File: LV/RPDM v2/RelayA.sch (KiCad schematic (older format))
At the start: 6 parts, among them K2 G8NW, Q2 Q_Dual_NMOS

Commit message: rPDM - Started on board layout
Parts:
- D4: renamed from D21; footprint (none) -> Diode_UOWM:TO-277_FSV10150V
- D5: renamed from D22; footprint (none) -> Diode_UOWM:TO-277_FSV10150V
- renumbered K2 to K3, Q2 to Q3, R24 to R14, R25 to R15
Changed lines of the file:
@@
 $Descr A4 11693 8268
 encoding utf-8
-Sheet 25 32
+Sheet 9 32
 Title "Relay Circuit"
 Date "2021-06-28"
@@
 Output
 $Comp
-L power:GND #PWR031
+L power:GND #PWR020
 U 1 1 6114E9D0
 P 6000 5000
-AR Path="/5E554D5D/5E5E9CA9/6114E9D0" Ref="#PWR031"  Part="1"
+AR Path="/5E554D5D/5E5E9CA9/6114E9D0" Ref="#PWR020"  Part="1"
 AR Path="/5E554D5D/5E5A0290/6114E9D0" Ref="#PWR?"  Part="1"
 AR Path="/5E554D5D/5E5A035E/6114E9D0" Ref="#PWR?"  Part="1"
@@
 AR Path="/5E554D5D/60DE7FBD/6114E9D0" Ref="#PWR?"  Part="1"
 AR Path="/5E554D5D/60DE88EB/6114E9D0" Ref="#PWR?"  Part="1"
-AR Path="/5E554D5D/60DED789/6114E9D0" Ref="#PWR026"  Part="1"
+AR Path="/5E554D5D/60DED789/6114E9D0" Ref="#PWR014"  Part="1"
 AR Path="/5E554D5D/60DEDCB5/6114E9D0" Ref="#PWR?"  Part="1"
 AR Path="/60E5EBEF/6114E9D0" Ref="#PWR?"  Part="1"
-F 0 "#PWR026" H 6000 4750 50  0001 C CNN
+F 0 "#PWR020" H 6000 4750 50  0001 C CNN
 F 1 "GND" H 6005 4827 50  0000 C CNN
 F 2 "" H 6000 5000 50  0001 C CNN
@@
 	6000 5000 6000 4700
 $Comp
-L Device2:R R24
+L Device2:R R14
 U 1 1 6183CC28
 P 5000 4750
-AR Path="/5E554D5D/5E5E9CA9/6183CC28" Ref="R24"  Part="1"
-AR Path="/5E554D5D/60DED789/6183CC28" Ref="R21"  Part="1"
+AR Path="/5E554D5D/5E5E9CA9/6183CC28" Ref="R14"  Part="1"
+AR Path="/5E554D5D/60DED789/6183CC28" Ref="R10"  Part="1"
 AR Path="/5E554D5D/60DE88EB/6183CC28" Ref="R?"  Part="1"
 AR Path="/5E554D5D/60DEDCB5/6183CC28" Ref="R?"  Part="1"
-F 0 "R21" H 5070 4796 50  0000 L CNN
+F 0 "R14" H 5070 4796 50  0000 L CNN
 F 1 "100k" H 5070 4705 50  0000 L CNN
 F 2 "Resistor_SMD:R_0805_2012Metric_Pad1.15x1.40mm_HandSolder" V 4930 4750 50  0001 C CNN
@@
 	5000 4900 5000 5000
 $Comp
-L power:GND #PWR030
+L power:GND #PWR019
 U 1 1 6114E9D3
 P 5000 5000
-AR Path="/5E554D5D/5E5E9CA9/6114E9D3" Ref="#PWR030"  Part="1"
+AR Path="/5E554D5D/5E5E9CA9/6114E9D3" Ref="#PWR019"  Part="1"
 AR Path="/5E554D5D/5E5A0290/6114E9D3" Ref="#PWR?"  Part="1"
 AR Path="/5E554D5D/5E5A035E/6114E9D3" Ref="#PWR?"  Part="1"
@@
 AR Path="/5E554D5D/60DE7FBD/6114E9D3" Ref="#PWR?"  Part="1"
 AR Path="/5E554D5D/60DE88EB/6114E9D3" Ref="#PWR?"  Part="1"
-AR Path="/5E554D5D/60DED789/6114E9D3" Ref="#PWR025"  Part="1"
+AR Path="/5E554D5D/60DED789/6114E9D3" Ref="#PWR013"  Part="1"
 AR Path="/5E554D5D/60DEDCB5/6114E9D3" Ref="#PWR?"  Part="1"
 AR Path="/60E5EBEF/6114E9D3" Ref="#PWR?"  Part="1"
-F 0 "#PWR025" H 5000 4750 50  0001 C CNN
+F 0 "#PWR019" H 5000 4750 50  0001 C CNN
 F 1 "GND" H 5005 4827 50  0000 C CNN
 F 2 "" H 5000 5000 50  0001 C CNN
@@
 	5000 4600 5000 4500
 $Comp
-L Device2:Q_Dual_NMOS_S1G1S2G2D2D2D1D1 Q2
+L Device2:Q_Dual_NMOS_S1G1S2G2D2D2D1D1 Q3
 U 1 1 6114E9D1
 P 5900 4500
-AR Path="/5E554D5D/5E5E9CA9/6114E9D1" Ref="Q2"  Part="1"
+AR Path="/5E554D5D/5E5E9CA9/6114E9D1" Ref="Q3"  Part="1"
 AR Path="/5E554D5D/60DE88EB/6114E9D1" Ref="Q?"  Part="1"
-AR Path="/5E554D5D/60DED789/6114E9D1" Ref="Q1"  Part="1"
-F 0 "Q1" H 6188 4546 50  0000 L CNN
+AR Path="/5E554D5D/60DED789/6114E9D1" Ref="Q2"  Part="1"
+F 0 "Q3" H 6188 4546 50  0000 L CNN
 F 1 "Q_Dual_NMOS" H 6188 4455 50  0000 L CNN
 F 2 "" H 6100 4500 50  0001 C CNN
@@
 $EndComp
 $Comp
-L relay_omron:G8NW K2
+L relay_omron:G8NW K3
 U 1 1 61724099
 P 5500 3300
-AR Path="/5E554D5D/5E5E9CA9/61724099" Ref="K2"  Part="1"
-AR Path="/5E554D5D/60DED789/61724099" Ref="K1"  Part="1"
-F 0 "K1" V 6067 3300 50  0000 C CNN
+AR Path="/5E554D5D/5E5E9CA9/61724099" Ref="K3"  Part="1"
+AR Path="/5E554D5D/60DED789/61724099" Ref="K2"  Part="1"
+F 0 "K3" V 6067 3300 50  0000 C CNN
 F 1 "G8NW" V 5976 3300 50  0000 C CNN
 F 2 "" H 5900 3200 50  0001 L CNN
@@
 $EndComp
 $Comp
-L Device2:R R25
+L Device2:R R15
 U 1 1 6174AD0B
 P 5500 4500
-AR Path="/5E554D5D/5E5E9CA9/6174AD0B" Ref="R25"  Part="1"
-AR Path="/5E554D5D/60DED789/6174AD0B" Ref="R22"  Part="1"
-F 0 "R22" V 5293 4500 50  0000 C CNN
+AR Path="/5E554D5D/5E5E9CA9/6174AD0B" Ref="R15"  Part="1"
+AR Path="/5E554D5D/60DED789/6174AD0B" Ref="R11"  Part="1"
+F 0 "R15" V 5293 4500 50  0000 C CNN
 F 1 "470" V 5384 4500 50  0000 C CNN
 F 2 "Resistor_SMD:R_0805_2012Metric_Pad1.15x1.40mm_HandSolder" V 5430 4500 50  0001 C CNN
@@
 $EndComp
 $Comp
-L power:GND #PWR032
+L power:GND #PWR021
 U 1 1 617CD98D
 P 6500 4000
-AR Path="/5E554D5D/5E5E9CA9/617CD98D" Ref="#PWR032"  Part="1"
+AR Path="/5E554D5D/5E5E9CA9/617CD98D" Ref="#PWR021"  Part="1"
 AR Path="/5E554D5D/5E5A0290/617CD98D" Ref="#PWR?"  Part="1"
 AR Path="/5E554D5D/5E5A035E/617CD98D" Ref="#PWR?"  Part="1"
@@
 AR Path="/5E554D5D/60DE7FBD/617CD98D" Ref="#PWR?"  Part="1"
 AR Path="/5E554D5D/60DE88EB/617CD98D" Ref="#PWR?"  Part="1"
-AR Path="/5E554D5D/60DED789/617CD98D" Ref="#PWR027"  Part="1"
+AR Path="/5E554D5D/60DED789/617CD98D" Ref="#PWR015"  Part="1"
 AR Path="/5E554D5D/60DEDCB5/617CD98D" Ref="#PWR?"  Part="1"
 AR Path="/60E5EBEF/617CD98D" Ref="#PWR?"  Part="1"
-F 0 "#PWR027" H 6500 3750 50  0001 C CNN
+F 0 "#PWR021" H 6500 3750 50  0001 C CNN
 F 1 "GND" H 6505 3827 50  0000 C CNN
 F 2 "" H 6500 4000 50  0001 C CNN
@@
 $EndComp
 $Comp
-L Device2:D_Schottky_AAK D21
+L Device2:D_Schottky_AAK D4
 U 1 1 617CF33C
 P 5500 4000
-AR Path="/5E554D5D/60DED789/617CF33C" Ref="D21"  Part="1"
-AR Path="/5E554D5D/5E5E9CA9/617CF33C" Ref="D24"  Part="1"
-F 0 "D21" H 5500 4100 50  0000 C CNN
+AR Path="/5E554D5D/60DED789/617CF33C" Ref="D4"  Part="1"
+AR Path="/5E554D5D/5E5E9CA9/617CF33C" Ref="D8"  Part="1"
+F 0 "D8" H 5500 4100 50  0000 C CNN
 F 1 "D_Schottky_Flyback" H 5450 3900 50  0000 C CNN
-F 2 "" H 5500 4000 50  0001 C CNN
+F 2 "Diode_UOWM:TO-277_FSV10150V" H 5500 4000 50  0001 C CNN
 F 3 "~" H 5500 4000 50  0001 C CNN
 	1    5500 4000
@@
 $EndComp
 $Comp
-L Device2:D_Schottky_AAK D22
+L Device2:D_Schottky_AAK D5
 U 1 1 617CFABC
 P 6500 3500
-AR Path="/5E554D5D/60DED789/617CFABC" Ref="D22"  Part="1"
-AR Path="/5E554D5D/5E5E9CA9/617CFABC" Ref="D25"  Part="1"
-F 0 "D22" V 6479 3644 50  0000 L CNN
+AR Path="/5E554D5D/60DED789/617CFABC" Ref="D5"  Part="1"
+AR Path="/5E554D5D/5E5E9CA9/617CFABC" Ref="D9"  Part="1"
+F 0 "D9" V 6479 3644 50  0000 L CNN
 F 1 "D_Schottky_Flyback" V 6570 3644 50  0000 L CNN
-F 2 "" H 6500 3500 50  0001 C CNN
+F 2 "Diode_UOWM:TO-277_FSV10150V" H 6500 3500 50  0001 C CNN
 F 3 "~" H 6500 3500 50  0001 C CNN
 	1    6500 3500

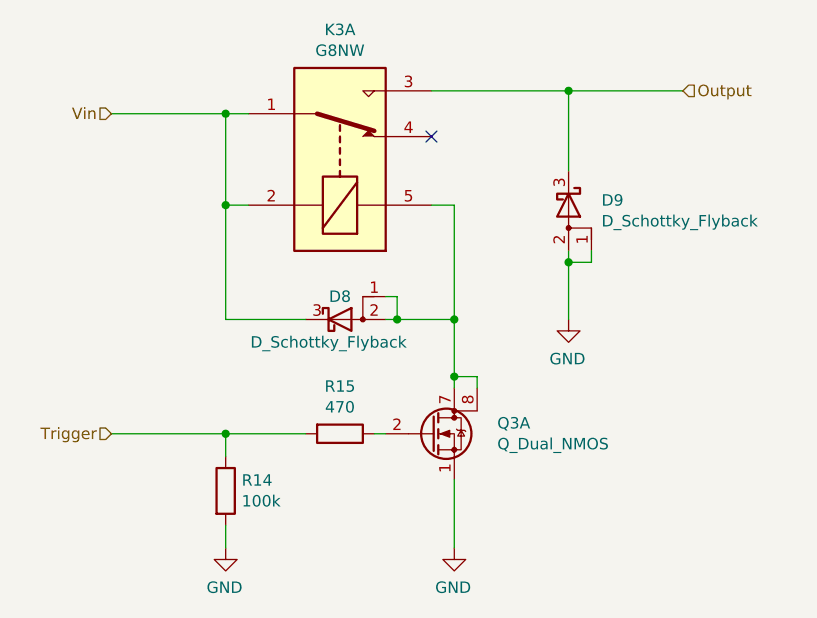
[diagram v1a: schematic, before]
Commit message: rpdm, libraries cleanup
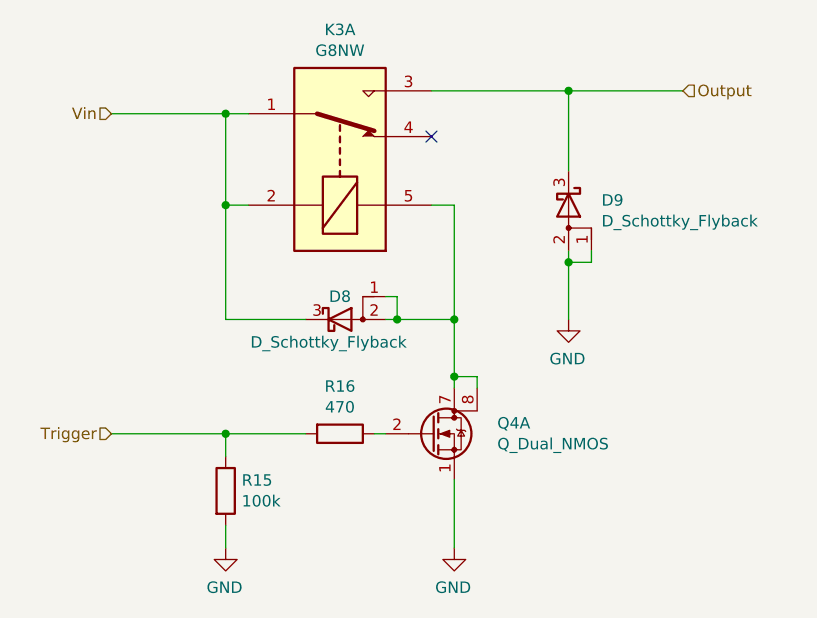
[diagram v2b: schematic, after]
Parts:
- renumbered Q3 to Q4, R14 to R15, R15 to R16
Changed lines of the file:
@@
 	6000 5000 6000 4700
 $Comp
-L Device2:R R14
+L Device2:R R15
 U 1 1 6183CC28
 P 5000 4750
-AR Path="/5E554D5D/5E5E9CA9/6183CC28" Ref="R14"  Part="1"
-AR Path="/5E554D5D/60DED789/6183CC28" Ref="R10"  Part="1"
+AR Path="/5E554D5D/5E5E9CA9/6183CC28" Ref="R15"  Part="1"
+AR Path="/5E554D5D/60DED789/6183CC28" Ref="R11"  Part="1"
 AR Path="/5E554D5D/60DE88EB/6183CC28" Ref="R?"  Part="1"
 AR Path="/5E554D5D/60DEDCB5/6183CC28" Ref="R?"  Part="1"
-F 0 "R14" H 5070 4796 50  0000 L CNN
+F 0 "R15" H 5070 4796 50  0000 L CNN
 F 1 "100k" H 5070 4705 50  0000 L CNN
 F 2 "Resistor_SMD:R_0805_2012Metric_Pad1.15x1.40mm_HandSolder" V 4930 4750 50  0001 C CNN
@@
 	5000 4600 5000 4500
 $Comp
-L Device2:Q_Dual_NMOS_S1G1S2G2D2D2D1D1 Q3
+L Device2:Q_Dual_NMOS_S1G1S2G2D2D2D1D1 Q4
 U 1 1 6114E9D1
 P 5900 4500
-AR Path="/5E554D5D/5E5E9CA9/6114E9D1" Ref="Q3"  Part="1"
+AR Path="/5E554D5D/5E5E9CA9/6114E9D1" Ref="Q4"  Part="1"
 AR Path="/5E554D5D/60DE88EB/6114E9D1" Ref="Q?"  Part="1"
-AR Path="/5E554D5D/60DED789/6114E9D1" Ref="Q2"  Part="1"
-F 0 "Q3" H 6188 4546 50  0000 L CNN
+AR Path="/5E554D5D/60DED789/6114E9D1" Ref="Q3"  Part="1"
+F 0 "Q4" H 6188 4546 50  0000 L CNN
 F 1 "Q_Dual_NMOS" H 6188 4455 50  0000 L CNN
 F 2 "" H 6100 4500 50  0001 C CNN
@@
 $EndComp
 $Comp
-L Device2:R R15
+L Device2:R R16
 U 1 1 6174AD0B
 P 5500 4500
-AR Path="/5E554D5D/5E5E9CA9/6174AD0B" Ref="R15"  Part="1"
-AR Path="/5E554D5D/60DED789/6174AD0B" Ref="R11"  Part="1"
-F 0 "R15" V 5293 4500 50  0000 C CNN
+AR Path="/5E554D5D/5E5E9CA9/6174AD0B" Ref="R16"  Part="1"
+AR Path="/5E554D5D/60DED789/6174AD0B" Ref="R12"  Part="1"
+F 0 "R16" V 5293 4500 50  0000 C CNN
 F 1 "470" V 5384 4500 50  0000 C CNN
 F 2 "Resistor_SMD:R_0805_2012Metric_Pad1.15x1.40mm_HandSolder" V 5430 4500 50  0001 C CNN

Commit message: RPDM
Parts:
- D1: renamed from D4; footprint Diode_UOWM:TO-277_FSV10150V -> UOWM_Diodes:TO-277_FSV10150V
- D2: renamed from D5; footprint Diode_UOWM:TO-277_FSV10150V -> UOWM_Diodes:TO-277_FSV10150V
- K2: renamed from K3; footprint (none) -> UOWM_Relays:Omron-G8NW-2L-AS_SK-MFG
- Q3: renamed from Q4; footprint (none) -> UOWM_Package_SO:Diodes_SO-8_5.3x6.2mm_P1.27mm
- renumbered R15 to R12, R16 to R13
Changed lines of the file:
@@
 $Descr A4 11693 8268
 encoding utf-8
-Sheet 9 32
+Sheet 29 30
 Title "Relay Circuit"
 Date "2021-06-28"
@@
 Output
 $Comp
-L power:GND #PWR020
+L power:GND #PWR017
 U 1 1 6114E9D0
 P 6000 5000
-AR Path="/5E554D5D/5E5E9CA9/6114E9D0" Ref="#PWR020"  Part="1"
+AR Path="/5E554D5D/5E5E9CA9/6114E9D0" Ref="#PWR017"  Part="1"
 AR Path="/5E554D5D/5E5A0290/6114E9D0" Ref="#PWR?"  Part="1"
 AR Path="/5E554D5D/5E5A035E/6114E9D0" Ref="#PWR?"  Part="1"
@@
 AR Path="/5E554D5D/60DE7FBD/6114E9D0" Ref="#PWR?"  Part="1"
 AR Path="/5E554D5D/60DE88EB/6114E9D0" Ref="#PWR?"  Part="1"
-AR Path="/5E554D5D/60DED789/6114E9D0" Ref="#PWR014"  Part="1"
+AR Path="/5E554D5D/60DED789/6114E9D0" Ref="#PWR011"  Part="1"
 AR Path="/5E554D5D/60DEDCB5/6114E9D0" Ref="#PWR?"  Part="1"
 AR Path="/60E5EBEF/6114E9D0" Ref="#PWR?"  Part="1"
-F 0 "#PWR020" H 6000 4750 50  0001 C CNN
+F 0 "#PWR017" H 6000 4750 50  0001 C CNN
 F 1 "GND" H 6005 4827 50  0000 C CNN
 F 2 "" H 6000 5000 50  0001 C CNN
@@
 	6000 5000 6000 4700
 $Comp
-L Device2:R R15
+L Device2:R R12
 U 1 1 6183CC28
 P 5000 4750
-AR Path="/5E554D5D/5E5E9CA9/6183CC28" Ref="R15"  Part="1"
-AR Path="/5E554D5D/60DED789/6183CC28" Ref="R11"  Part="1"
+AR Path="/5E554D5D/5E5E9CA9/6183CC28" Ref="R12"  Part="1"
+AR Path="/5E554D5D/60DED789/6183CC28" Ref="R8"  Part="1"
 AR Path="/5E554D5D/60DE88EB/6183CC28" Ref="R?"  Part="1"
 AR Path="/5E554D5D/60DEDCB5/6183CC28" Ref="R?"  Part="1"
-F 0 "R15" H 5070 4796 50  0000 L CNN
+F 0 "R12" H 5070 4796 50  0000 L CNN
 F 1 "100k" H 5070 4705 50  0000 L CNN
 F 2 "Resistor_SMD:R_0805_2012Metric_Pad1.15x1.40mm_HandSolder" V 4930 4750 50  0001 C CNN
-F 3 "~" H 5000 4750 50  0001 C CNN
+F 3 "https://www.koaspeer.com/pdfs/RK73H.pdf" H 5000 4750 50  0001 C CNN
 	1    5000 4750
 	1    0    0    -1
@@
 	5000 4900 5000 5000
 $Comp
-L power:GND #PWR019
+L power:GND #PWR016
 U 1 1 6114E9D3
 P 5000 5000
-AR Path="/5E554D5D/5E5E9CA9/6114E9D3" Ref="#PWR019"  Part="1"
+AR Path="/5E554D5D/5E5E9CA9/6114E9D3" Ref="#PWR016"  Part="1"
 AR Path="/5E554D5D/5E5A0290/6114E9D3" Ref="#PWR?"  Part="1"
 AR Path="/5E554D5D/5E5A035E/6114E9D3" Ref="#PWR?"  Part="1"
@@
 AR Path="/5E554D5D/60DE7FBD/6114E9D3" Ref="#PWR?"  Part="1"
 AR Path="/5E554D5D/60DE88EB/6114E9D3" Ref="#PWR?"  Part="1"
-AR Path="/5E554D5D/60DED789/6114E9D3" Ref="#PWR013"  Part="1"
+AR Path="/5E554D5D/60DED789/6114E9D3" Ref="#PWR010"  Part="1"
 AR Path="/5E554D5D/60DEDCB5/6114E9D3" Ref="#PWR?"  Part="1"
 AR Path="/60E5EBEF/6114E9D3" Ref="#PWR?"  Part="1"
-F 0 "#PWR019" H 5000 4750 50  0001 C CNN
+F 0 "#PWR016" H 5000 4750 50  0001 C CNN
 F 1 "GND" H 5005 4827 50  0000 C CNN
 F 2 "" H 5000 5000 50  0001 C CNN
@@
 	5000 4600 5000 4500
 $Comp
-L Device2:Q_Dual_NMOS_S1G1S2G2D2D2D1D1 Q4
+L Device2:Q_Dual_NMOS_S1G1S2G2D2D2D1D1 Q3
 U 1 1 6114E9D1
 P 5900 4500
-AR Path="/5E554D5D/5E5E9CA9/6114E9D1" Ref="Q4"  Part="1"
+AR Path="/5E554D5D/5E5E9CA9/6114E9D1" Ref="Q3"  Part="1"
 AR Path="/5E554D5D/60DE88EB/6114E9D1" Ref="Q?"  Part="1"
-AR Path="/5E554D5D/60DED789/6114E9D1" Ref="Q3"  Part="1"
-F 0 "Q4" H 6188 4546 50  0000 L CNN
+AR Path="/5E554D5D/60DED789/6114E9D1" Ref="Q2"  Part="1"
+F 0 "Q3" H 6188 4546 50  0000 L CNN
 F 1 "Q_Dual_NMOS" H 6188 4455 50  0000 L CNN
-F 2 "" H 6100 4500 50  0001 C CNN
-F 3 "~" H 6100 4500 50  0001 C CNN
+F 2 "UOWM_Package_SO:Diodes_SO-8_5.3x6.2mm_P1.27mm" H 6100 4500 50  0001 C CNN
+F 3 "https://www.diodes.com/assets/Datasheets/DMT3020LSDQ.pdf" H 6100 4500 50  0001 C CNN
 	1    5900 4500
 	1    0    0    -1
 $EndComp
 $Comp
-L relay_omron:G8NW K3
+L relay_omron:G8NW K2
 U 1 1 61724099
 P 5500 3300
-AR Path="/5E554D5D/5E5E9CA9/61724099" Ref="K3"  Part="1"
-AR Path="/5E554D5D/60DED789/61724099" Ref="K2"  Part="1"
-F 0 "K3" V 6067 3300 50  0000 C CNN
+AR Path="/5E554D5D/5E5E9CA9/61724099" Ref="K2"  Part="1"
+AR Path="/5E554D5D/60DED789/61724099" Ref="K1"  Part="1"
+F 0 "K2" V 6067 3300 50  0000 C CNN
 F 1 "G8NW" V 5976 3300 50  0000 C CNN
-F 2 "" H 5900 3200 50  0001 L CNN
+F 2 "UOWM_Relays:Omron-G8NW-2L-AS_SK-MFG" H 5900 3200 50  0001 L CNN
 F 3 "https://omronfs.omron.com/en_US/ecb/products/pdf/en-g8nw.pdf" H 5900 3400 50  0001 C CNN
 	1    5500 3300
@@
 $EndComp
 $Comp
-L Device2:R R16
+L Device2:R R13
 U 1 1 6174AD0B
 P 5500 4500
-AR Path="/5E554D5D/5E5E9CA9/6174AD0B" Ref="R16"  Part="1"
-AR Path="/5E554D5D/60DED789/6174AD0B" Ref="R12"  Part="1"
-F 0 "R16" V 5293 4500 50  0000 C CNN
+AR Path="/5E554D5D/5E5E9CA9/6174AD0B" Ref="R13"  Part="1"
+AR Path="/5E554D5D/60DED789/6174AD0B" Ref="R9"  Part="1"
+F 0 "R13" V 5293 4500 50  0000 C CNN
 F 1 "470" V 5384 4500 50  0000 C CNN
 F 2 "Resistor_SMD:R_0805_2012Metric_Pad1.15x1.40mm_HandSolder" V 5430 4500 50  0001 C CNN
@@
 $EndComp
 $Comp
-L power:GND #PWR021
+L power:GND #PWR018
 U 1 1 617CD98D
 P 6500 4000
-AR Path="/5E554D5D/5E5E9CA9/617CD98D" Ref="#PWR021"  Part="1"
+AR Path="/5E554D5D/5E5E9CA9/617CD98D" Ref="#PWR018"  Part="1"
 AR Path="/5E554D5D/5E5A0290/617CD98D" Ref="#PWR?"  Part="1"
 AR Path="/5E554D5D/5E5A035E/617CD98D" Ref="#PWR?"  Part="1"
@@
 AR Path="/5E554D5D/60DE7FBD/617CD98D" Ref="#PWR?"  Part="1"
 AR Path="/5E554D5D/60DE88EB/617CD98D" Ref="#PWR?"  Part="1"
-AR Path="/5E554D5D/60DED789/617CD98D" Ref="#PWR015"  Part="1"
+AR Path="/5E554D5D/60DED789/617CD98D" Ref="#PWR012"  Part="1"
 AR Path="/5E554D5D/60DEDCB5/617CD98D" Ref="#PWR?"  Part="1"
 AR Path="/60E5EBEF/617CD98D" Ref="#PWR?"  Part="1"
-F 0 "#PWR021" H 6500 3750 50  0001 C CNN
+F 0 "#PWR018" H 6500 3750 50  0001 C CNN
 F 1 "GND" H 6505 3827 50  0000 C CNN
 F 2 "" H 6500 4000 50  0001 C CNN
@@
 $EndComp
 $Comp
-L Device2:D_Schottky_AAK D4
+L Device2:D_Schottky_AAK D1
 U 1 1 617CF33C
 P 5500 4000
-AR Path="/5E554D5D/60DED789/617CF33C" Ref="D4"  Part="1"
-AR Path="/5E554D5D/5E5E9CA9/617CF33C" Ref="D8"  Part="1"
-F 0 "D8" H 5500 4100 50  0000 C CNN
+AR Path="/5E554D5D/60DED789/617CF33C" Ref="D1"  Part="1"
+AR Path="/5E554D5D/5E5E9CA9/617CF33C" Ref="D5"  Part="1"
+F 0 "D5" H 5500 4100 50  0000 C CNN
 F 1 "D_Schottky_Flyback" H 5450 3900 50  0000 C CNN
-F 2 "Diode_UOWM:TO-277_FSV10150V" H 5500 4000 50  0001 C CNN
+F 2 "UOWM_Diodes:TO-277_FSV10150V" H 5500 4000 50  0001 C CNN
 F 3 "~" H 5500 4000 50  0001 C CNN
 	1    5500 4000
@@
 $EndComp
 $Comp
-L Device2:D_Schottky_AAK D5
+L Device2:D_Schottky_AAK D2
 U 1 1 617CFABC
 P 6500 3500
-AR Path="/5E554D5D/60DED789/617CFABC" Ref="D5"  Part="1"
-AR Path="/5E554D5D/5E5E9CA9/617CFABC" Ref="D9"  Part="1"
-F 0 "D9" V 6479 3644 50  0000 L CNN
+AR Path="/5E554D5D/60DED789/617CFABC" Ref="D2"  Part="1"
+AR Path="/5E554D5D/5E5E9CA9/617CFABC" Ref="D6"  Part="1"
+F 0 "D6" V 6479 3644 50  0000 L CNN
 F 1 "D_Schottky_Flyback" V 6570 3644 50  0000 L CNN
-F 2 "Diode_UOWM:TO-277_FSV10150V" H 6500 3500 50  0001 C CNN
+F 2 "UOWM_Diodes:TO-277_FSV10150V" H 6500 3500 50  0001 C CNN
 F 3 "~" H 6500 3500 50  0001 C CNN
 	1    6500 3500

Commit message: RPDM nearly finished
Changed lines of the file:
@@
 $Descr A4 11693 8268
 encoding utf-8
-Sheet 29 30
+Sheet 27 30
 Title "Relay Circuit"
 Date "2021-06-28"
@@
 AR Path="/5E554D5D/60DE88EB/6183CC28" Ref="R?"  Part="1"
 AR Path="/5E554D5D/60DEDCB5/6183CC28" Ref="R?"  Part="1"
-F 0 "R12" H 5070 4796 50  0000 L CNN
+F 0 "R8" H 5070 4796 50  0000 L CNN
 F 1 "100k" H 5070 4705 50  0000 L CNN
 F 2 "Resistor_SMD:R_0805_2012Metric_Pad1.15x1.40mm_HandSolder" V 4930 4750 50  0001 C CNN
@@
 AR Path="/5E554D5D/60DE88EB/6114E9D1" Ref="Q?"  Part="1"
 AR Path="/5E554D5D/60DED789/6114E9D1" Ref="Q2"  Part="1"
-F 0 "Q3" H 6188 4546 50  0000 L CNN
+F 0 "Q2" H 6188 4546 50  0000 L CNN
 F 1 "Q_Dual_NMOS" H 6188 4455 50  0000 L CNN
 F 2 "UOWM_Package_SO:Diodes_SO-8_5.3x6.2mm_P1.27mm" H 6100 4500 50  0001 C CNN
@@
 AR Path="/5E554D5D/5E5E9CA9/61724099" Ref="K2"  Part="1"
 AR Path="/5E554D5D/60DED789/61724099" Ref="K1"  Part="1"
-F 0 "K2" V 6067 3300 50  0000 C CNN
+F 0 "K1" V 6067 3300 50  0000 C CNN
 F 1 "G8NW" V 5976 3300 50  0000 C CNN
 F 2 "UOWM_Relays:Omron-G8NW-2L-AS_SK-MFG" H 5900 3200 50  0001 L CNN
@@
 AR Path="/5E554D5D/5E5E9CA9/6174AD0B" Ref="R13"  Part="1"
 AR Path="/5E554D5D/60DED789/6174AD0B" Ref="R9"  Part="1"
-F 0 "R13" V 5293 4500 50  0000 C CNN
+F 0 "R9" V 5293 4500 50  0000 C CNN
 F 1 "470" V 5384 4500 50  0000 C CNN
 F 2 "Resistor_SMD:R_0805_2012Metric_Pad1.15x1.40mm_HandSolder" V 5430 4500 50  0001 C CNN
@@
 AR Path="/5E554D5D/60DED789/617CF33C" Ref="D1"  Part="1"
 AR Path="/5E554D5D/5E5E9CA9/617CF33C" Ref="D5"  Part="1"
-F 0 "D5" H 5500 4100 50  0000 C CNN
+F 0 "D1" H 5500 4100 50  0000 C CNN
 F 1 "D_Schottky_Flyback" H 5450 3900 50  0000 C CNN
 F 2 "UOWM_Diodes:TO-277_FSV10150V" H 5500 4000 50  0001 C CNN
@@
 AR Path="/5E554D5D/60DED789/617CFABC" Ref="D2"  Part="1"
 AR Path="/5E554D5D/5E5E9CA9/617CFABC" Ref="D6"  Part="1"
-F 0 "D6" V 6479 3644 50  0000 L CNN
+F 0 "D2" V 6479 3644 50  0000 L CNN
 F 1 "D_Schottky_Flyback" V 6570 3644 50  0000 L CNN
 F 2 "UOWM_Diodes:TO-277_FSV10150V" H 6500 3500 50  0001 C CNN

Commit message: RPDM
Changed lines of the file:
@@
 $Descr A4 11693 8268
 encoding utf-8
-Sheet 27 30
+Sheet 29 30
 Title "Relay Circuit"
 Date "2021-06-28"
@@
 AR Path="/5E554D5D/60DE88EB/6183CC28" Ref="R?"  Part="1"
 AR Path="/5E554D5D/60DEDCB5/6183CC28" Ref="R?"  Part="1"
-F 0 "R8" H 5070 4796 50  0000 L CNN
+F 0 "R12" H 5070 4796 50  0000 L CNN
 F 1 "100k" H 5070 4705 50  0000 L CNN
 F 2 "Resistor_SMD:R_0805_2012Metric_Pad1.15x1.40mm_HandSolder" V 4930 4750 50  0001 C CNN
@@
 AR Path="/5E554D5D/60DE88EB/6114E9D1" Ref="Q?"  Part="1"
 AR Path="/5E554D5D/60DED789/6114E9D1" Ref="Q2"  Part="1"
-F 0 "Q2" H 6188 4546 50  0000 L CNN
+F 0 "Q3" H 6188 4546 50  0000 L CNN
 F 1 "Q_Dual_NMOS" H 6188 4455 50  0000 L CNN
 F 2 "UOWM_Package_SO:Diodes_SO-8_5.3x6.2mm_P1.27mm" H 6100 4500 50  0001 C CNN
@@
 AR Path="/5E554D5D/5E5E9CA9/61724099" Ref="K2"  Part="1"
 AR Path="/5E554D5D/60DED789/61724099" Ref="K1"  Part="1"
-F 0 "K1" V 6067 3300 50  0000 C CNN
+F 0 "K2" V 6067 3300 50  0000 C CNN
 F 1 "G8NW" V 5976 3300 50  0000 C CNN
 F 2 "UOWM_Relays:Omron-G8NW-2L-AS_SK-MFG" H 5900 3200 50  0001 L CNN
@@
 AR Path="/5E554D5D/5E5E9CA9/6174AD0B" Ref="R13"  Part="1"
 AR Path="/5E554D5D/60DED789/6174AD0B" Ref="R9"  Part="1"
-F 0 "R9" V 5293 4500 50  0000 C CNN
+F 0 "R13" V 5293 4500 50  0000 C CNN
 F 1 "470" V 5384 4500 50  0000 C CNN
 F 2 "Resistor_SMD:R_0805_2012Metric_Pad1.15x1.40mm_HandSolder" V 5430 4500 50  0001 C CNN
@@
 AR Path="/5E554D5D/60DED789/617CF33C" Ref="D1"  Part="1"
 AR Path="/5E554D5D/5E5E9CA9/617CF33C" Ref="D5"  Part="1"
-F 0 "D1" H 5500 4100 50  0000 C CNN
+F 0 "D5" H 5500 4100 50  0000 C CNN
 F 1 "D_Schottky_Flyback" H 5450 3900 50  0000 C CNN
 F 2 "UOWM_Diodes:TO-277_FSV10150V" H 5500 4000 50  0001 C CNN
@@
 AR Path="/5E554D5D/60DED789/617CFABC" Ref="D2"  Part="1"
 AR Path="/5E554D5D/5E5E9CA9/617CFABC" Ref="D6"  Part="1"
-F 0 "D2" V 6479 3644 50  0000 L CNN
+F 0 "D6" V 6479 3644 50  0000 L CNN
 F 1 "D_Schottky_Flyback" V 6570 3644 50  0000 L CNN
 F 2 "UOWM_Diodes:TO-277_FSV10150V" H 6500 3500 50  0001 C CNN
